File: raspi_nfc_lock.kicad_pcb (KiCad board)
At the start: 2 copper layers, 79 parts, among them J101 Raspberry_Pi_2_3, J102 Screw_Terminal_01x02, J103 Screw_Terminal_01x02, J104 Screw_Terminal_01x02, J105 Screw_Terminal_01x02, J106 Screw_Terminal_01x02, J107 Screw_Terminal_01x02, J108 Screw_Terminal_01x02, J109 Screw_Terminal_01x02, J110 Screw_Terminal_01x02, J111 Screw_Terminal_01x02, J112 Screw_Terminal_01x02, J113 BUZZER, K101 G6E, Q101 MMBT3904, Q102 Si2319CDS, Q103 MMBT3904, U101 74HC14, U102 LM2596S, U103 TXB0104D

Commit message: Finished PCB design
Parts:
- D111: value PESD3V3L4UF -> SP0502BAHT; footprint Package_TO_SOT_SMD:SOT-886 -> Package_TO_SOT_SMD:SOT-23
- moved R129 105.7 mm to (155.5, 77.2), turned to 270 degrees
- moved J113 99.5 mm to (148.0, 64.5)
- moved Q103 98.4 mm to (153.5, 72.0), turned to 180 degrees
- moved R130 94.2 mm to (143.0, 73.5)
- moved R131 92.0 mm to (143.1, 70.5)
- moved C108 91.5 mm to (142.5, 93.2), turned to 0 degrees
- moved D108 86.1 mm to (102.0, 137.0), turned to 270 degrees
- moved D109 86.1 mm to (119.0, 131.8)
- moved R126 85.6 mm to (119.0, 126.8)
- moved R101 84.0 mm to (131.6, 115.8), turned to 90 degrees
- moved C101 83.9 mm to (143.2, 117.7)
- moved C102 83.9 mm to (143.9, 119.2)
- moved C103 83.9 mm to (145.4, 120.7)
- moved C104 83.9 mm to (150.2, 118.7)
- moved C105 83.9 mm to (151.7, 117.2)
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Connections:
- net Net-(D108-Pad1) renamed /LOCK_SOLENOID
- net Net-(F101-Pad2) renamed /PWR_IN
- net Net-(J110-Pad2) renamed /NFC_CS
- net Net-(J111-Pad1) renamed /NFC_MISO
- net Net-(J111-Pad2) renamed /NFC_MOSI
- net Net-(J112-Pad1) renamed /NFC_SCK
- net Net-(J113-Pad2) renamed /BUZZ
- D111 pad 1: /APA102_CLK -> /LED_CLK
- D111 pad 2: GND -> /LED_DATA
- D111 pad 3: /APA102_DATA -> GND
- J101 pad 32: (no net) -> /BUZZER
- J108 pad 2: Net-(J108-Pad2) -> /LED_DATA
- J109 pad 1: Net-(J109-Pad1) -> /LED_CLK
- R129 pad 2: (no net) -> /BUZZER
- R132 pad 1: Net-(J108-Pad2) -> /LED_DATA
- R133 pad 1: Net-(J109-Pad1) -> /LED_CLK
- U103 pad 8: (no net) -> +3V3
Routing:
- net +5V: track 23.3 -> 144.6 mm
- net +3V3: track 16.6 -> 113.9 mm, vias 3 -> 5
- net +12V: track 33.6 -> 123.5 mm, vias 0 -> 2
- net /DOOR_SW: track 2.13 -> 40.6 mm
- net /RELAY: track 0.00 -> 38.1 mm
- net /LOCK_SOLENOID: track 0.00 -> 34.6 mm
- net /LATCH_SW: track 3.43 -> 37.3 mm
- net /HANDLE: track 3.63 -> 30.6 mm, vias 1 -> 0
- net /DOOR: track 3.65 -> 30.6 mm, vias 1 -> 0
- net /*CE0: track 0.00 -> 26.1 mm
- net /LATCH: track 3.65 -> 29.5 mm, vias 1 -> 0
- net /HANDLE_SW: track 1.55 -> 26.3 mm
- net /BUTTON_1: track 4.78 -> 27.6 mm
- net /B1: track 3.89 -> 26.5 mm, vias 1 -> 2
- net /BUTTON_2: track 4.14 -> 25.8 mm
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- added copper zone on F.Cu, net GND

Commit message: Cleanups
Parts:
- D101, D108: footprint Diodes_SMD:D_SMB -> Diodes_SMD:D_SOD-123
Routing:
- net Net-(D101-Pad2): track 18.7 -> 16.1 mm, vias 1 -> 0

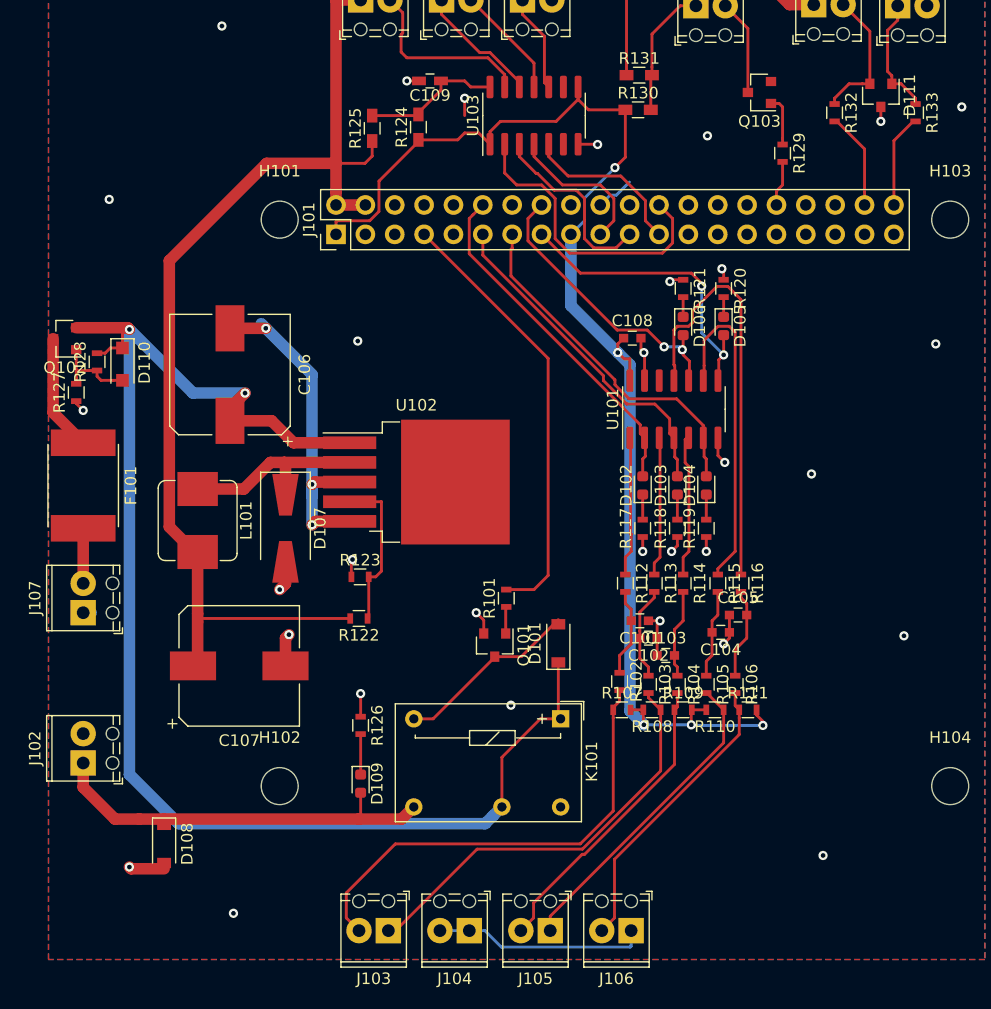
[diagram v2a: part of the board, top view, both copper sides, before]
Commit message: Moved silkprints away from pads
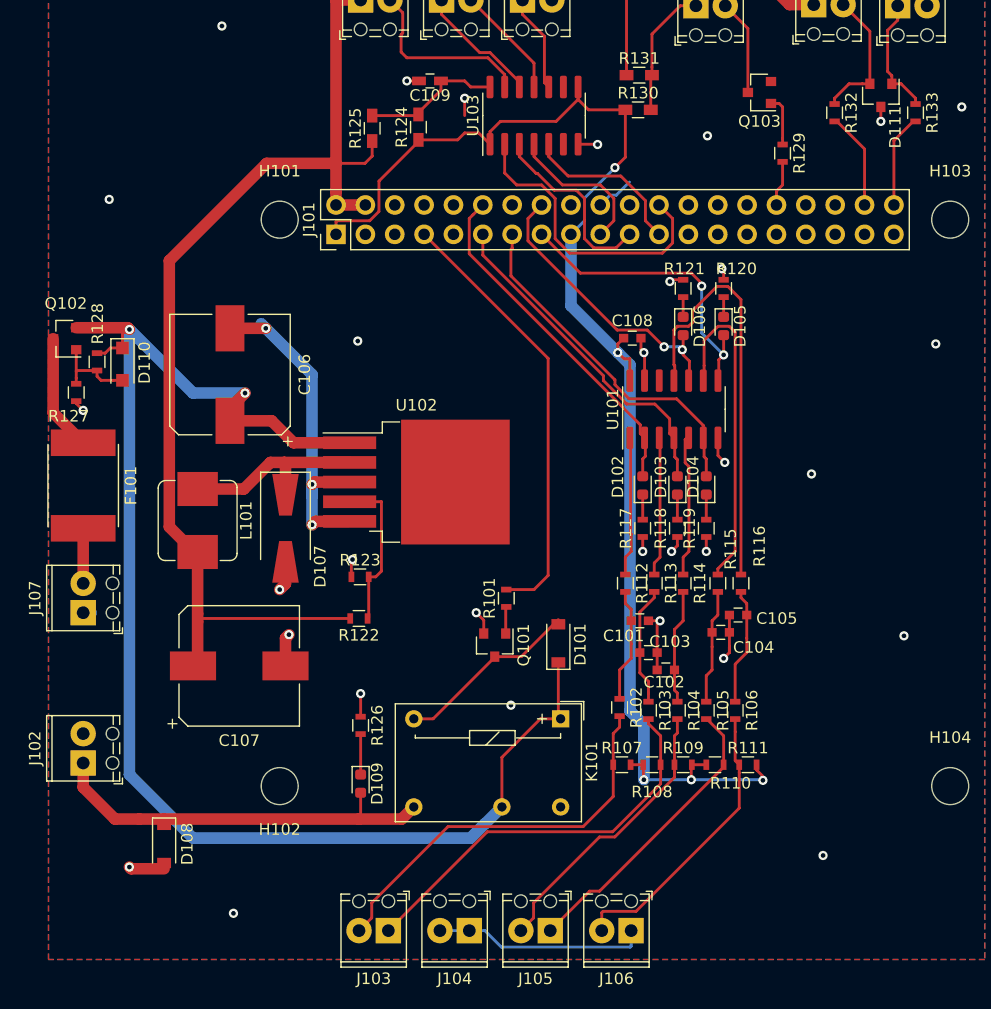
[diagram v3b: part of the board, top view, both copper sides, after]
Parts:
- moved R107 4.75 mm to (141.6, 130.2)
- moved R108 4.75 mm to (144.2, 130.2)
- moved R109 4.75 mm to (146.9, 130.2)
- moved R110 4.75 mm to (149.7, 130.2)
- moved R111 4.75 mm to (152.5, 130.2)
- moved R102 2.25 mm to (141.4, 125.2)
- moved R103 2.25 mm to (143.9, 125.5)
- moved R104 2.25 mm to (146.4, 125.5)
- moved R105 2.25 mm to (148.9, 125.5)
- moved R106 2.25 mm to (151.4, 125.5)
- moved C102 1.25 mm to (143.9, 120.5)
- moved C103 1.25 mm to (145.4, 122.0)
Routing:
- net /DOOR_SW: track 40.6 -> 35.1 mm
- net +3V3: track 113.9 -> 118.7 mm
- net GND: track 92.4 -> 95.4 mm
- net /LATCH_SW: track 37.3 -> 34.8 mm
- net Net-(C103-Pad2): track 7.66 -> 9.91 mm
- net Net-(C104-Pad2): track 7.66 -> 9.91 mm
- net Net-(C102-Pad2): track 8.08 -> 10.3 mm
- net Net-(C105-Pad2): track 7.87 -> 10.1 mm
- net Net-(C101-Pad2): track 7.62 -> 9.87 mm
- net /BUTTON_1: track 27.6 -> 25.7 mm
- net /HANDLE_SW: track 26.3 -> 24.7 mm
- net +12V: track 123.5 -> 124.5 mm
- net /BUTTON_2: track 25.8 -> 25.2 mm

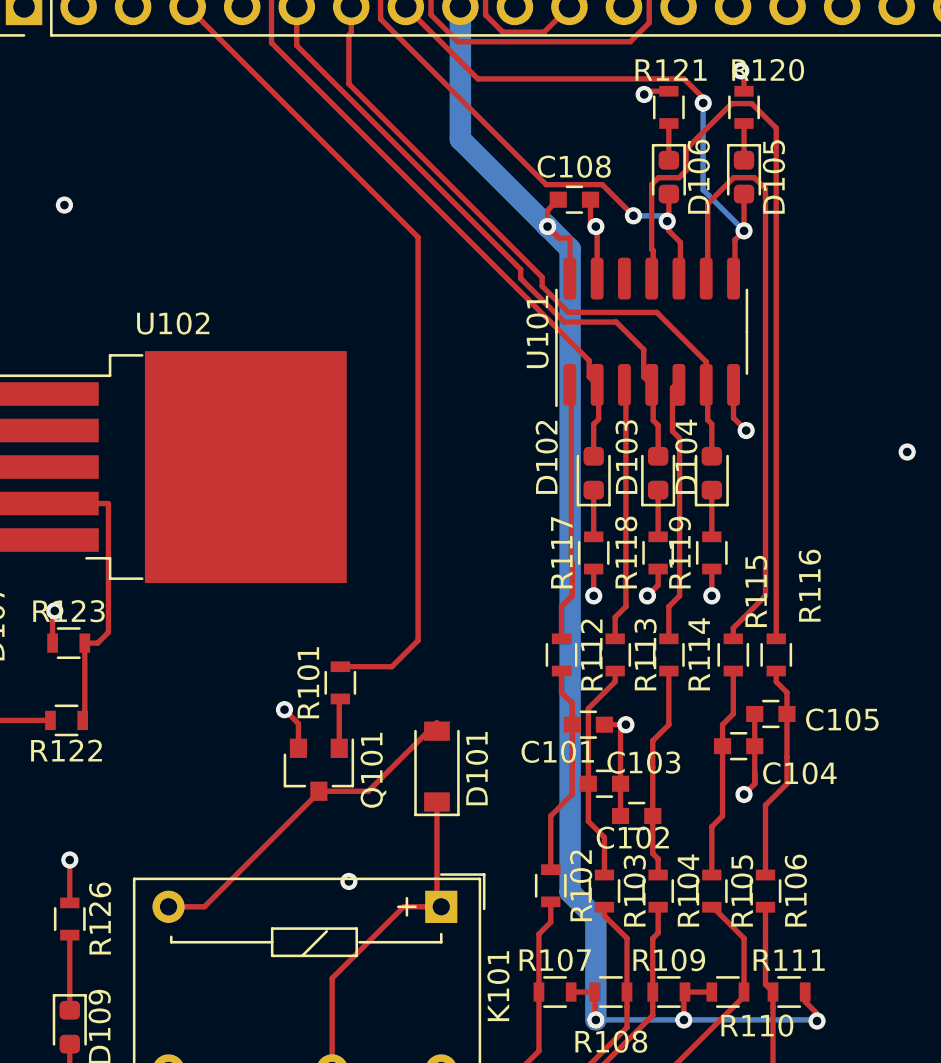
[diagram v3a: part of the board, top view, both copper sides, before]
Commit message: Removed thermals from regulator
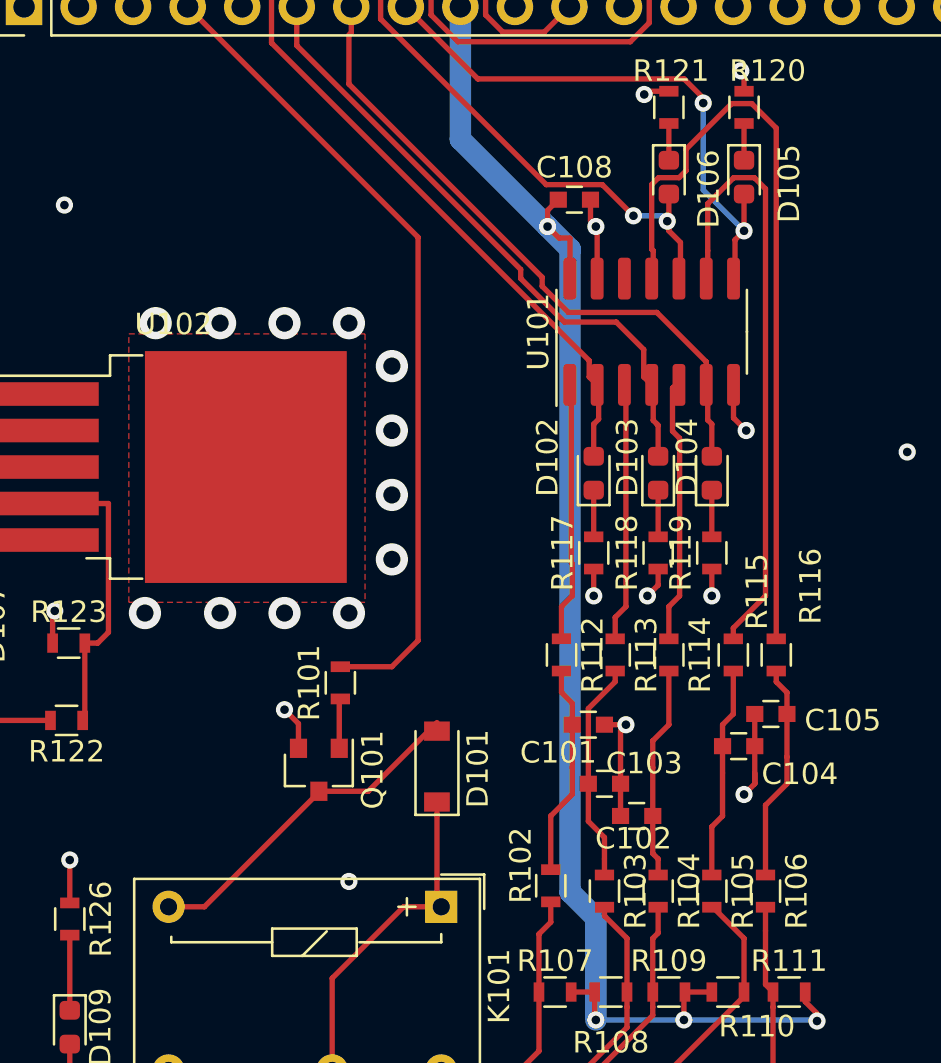
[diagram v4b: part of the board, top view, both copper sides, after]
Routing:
- net GND: vias 35 -> 47
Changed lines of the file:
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@@
     (thickness 1.6)
     (drawings 4)
-    (tracks 521)
+    (tracks 533)
     (zones 0)
     (modules 79)
@@
   (page A4)
   (layers
-    (0 F.Cu signal hide)
-    (31 B.Cu signal hide)
+    (0 F.Cu signal)
+    (31 B.Cu signal)
     (32 B.Adhes user)
     (33 F.Adhes user)
@@
     (tags "resistor 0603")
     (attr smd)
-    (fp_text reference R102 (at 0 -1.45 90) (layer F.SilkS)
+    (fp_text reference R102 (at -0.95 1.4 90) (layer F.SilkS)
       (effects (font (size 1 1) (thickness 0.15)))
     )
@@
     (tags diode)
     (attr smd)
-    (fp_text reference D106 (at 0 -1.43 90) (layer F.SilkS)
+    (fp_text reference D106 (at 0.55 -1.85 90) (layer F.SilkS)
       (effects (font (size 1 1) (thickness 0.15)))
     )
@@
     (tags diode)
     (attr smd)
-    (fp_text reference D105 (at 0 -1.43 90) (layer F.SilkS)
+    (fp_text reference D105 (at 0.3 -2.1 90) (layer F.SilkS)
       (effects (font (size 1 1) (thickness 0.15)))
     )
@@
   (segment (start 144.65 117.95) (end 144.9 117.7) (width 0.25) (layer F.Cu) (net 3))
   (segment (start 144.65 120.45) (end 144.65 117.95) (width 0.25) (layer F.Cu) (net 3))
+  (via (at 123 99) (size 1.5) (drill 0.8) (layers F.Cu B.Cu) (net 3))
+  (via (at 126 99) (size 1.5) (drill 0.8) (layers F.Cu B.Cu) (net 3))
+  (via (at 129 99) (size 1.5) (drill 0.8) (layers F.Cu B.Cu) (net 3))
+  (via (at 132 99) (size 1.5) (drill 0.8) (layers F.Cu B.Cu) (net 3))
+  (via (at 134 101) (size 1.5) (drill 0.8) (layers F.Cu B.Cu) (net 3))
+  (via (at 134 104) (size 1.5) (drill 0.8) (layers F.Cu B.Cu) (net 3))
+  (via (at 134 107) (size 1.5) (drill 0.8) (layers F.Cu B.Cu) (net 3))
+  (via (at 134 110) (size 1.5) (drill 0.8) (layers F.Cu B.Cu) (net 3))
+  (via (at 132 112.5) (size 1.5) (drill 0.8) (layers F.Cu B.Cu) (net 3))
+  (via (at 129 112.5) (size 1.5) (drill 0.8) (layers F.Cu B.Cu) (net 3))
+  (via (at 126 112.5) (size 1.5) (drill 0.8) (layers F.Cu B.Cu) (net 3))
+  (via (at 122.5 112.5) (size 1.5) (drill 0.8) (layers F.Cu B.Cu) (net 3))
   (segment (start 142.35 130.15) (end 143.45 130.15) (width 0.25) (layer F.Cu) (net 4) (status 30))
   (via (at 143.5 131.45) (size 0.8) (drill 0.4) (layers F.Cu B.Cu) (net 4))
@@
   (segment (start 118.05 104) (end 112.4 104) (width 1) (layer F.Cu) (net 31) (status 10))
   (segment (start 119 131) (end 119 127.5) (width 0.25) (layer F.Cu) (net 32) (status 30))
-  (segment (start 95 114.46) (end 95 109.7) (width 1) (layer F.Cu) (net 53) (status 30))
   (segment (start 92.4 99.7) (end 95 102.3) (width 1) (layer F.Cu) (net 33) (status 20))
   (segment (start 92.4 93.3) (end 92.4 99.7) (width 1) (layer F.Cu) (net 33) (status 10))
@@
   (segment (start 119 132.575) (end 119 134.7) (width 0.25) (layer F.Cu) (net 52) (status 10))
   (segment (start 122.55 134.85) (end 118.85 134.85) (width 1) (layer F.Cu) (net 52))
+  (segment (start 95 114.46) (end 95 109.7) (width 1) (layer F.Cu) (net 53) (status 30))
   (segment (start 163.05 66.71) (end 163.05 71.25) (width 0.25) (layer F.Cu) (net 54) (status 20))
   (segment (start 160.74 64.4) (end 163.05 66.71) (width 0.25) (layer F.Cu) (net 54) (status 10))
@@
       )
     )
+  )
+  (zone (net 3) (net_name GND) (layer F.Cu) (hatch edge 0.508)
+    (connect_pads thru_hole_only (clearance 0.5))
+    (min_thickness 0.254)
+    (fill yes (arc_segments 32) (thermal_gap 0.508) (thermal_bridge_width 0.508))
+    (polygon
+      (pts
+        (xy 121.75 99.5) (xy 132.75 99.5) (xy 132.75 112) (xy 121.75 112)
+      )
+    )

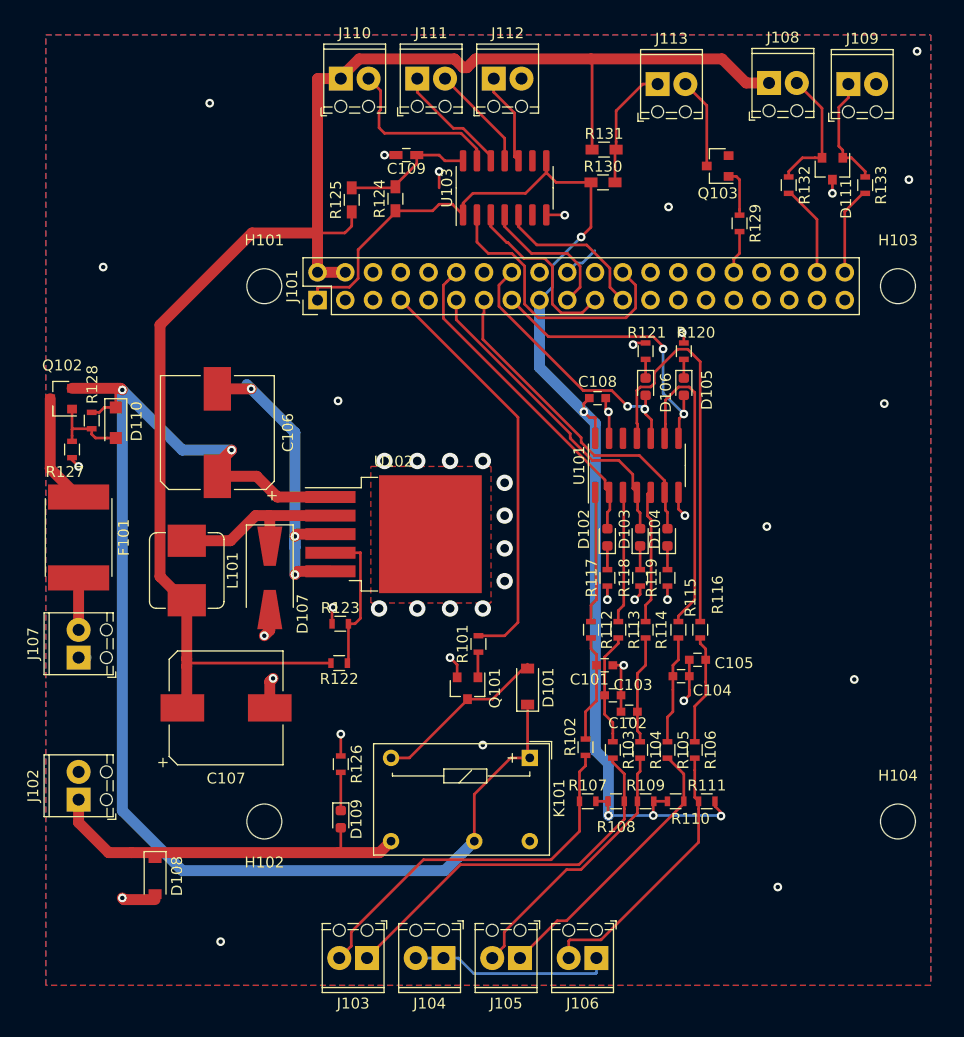
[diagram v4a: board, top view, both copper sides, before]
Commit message: Changed TX0104 to TSSOP
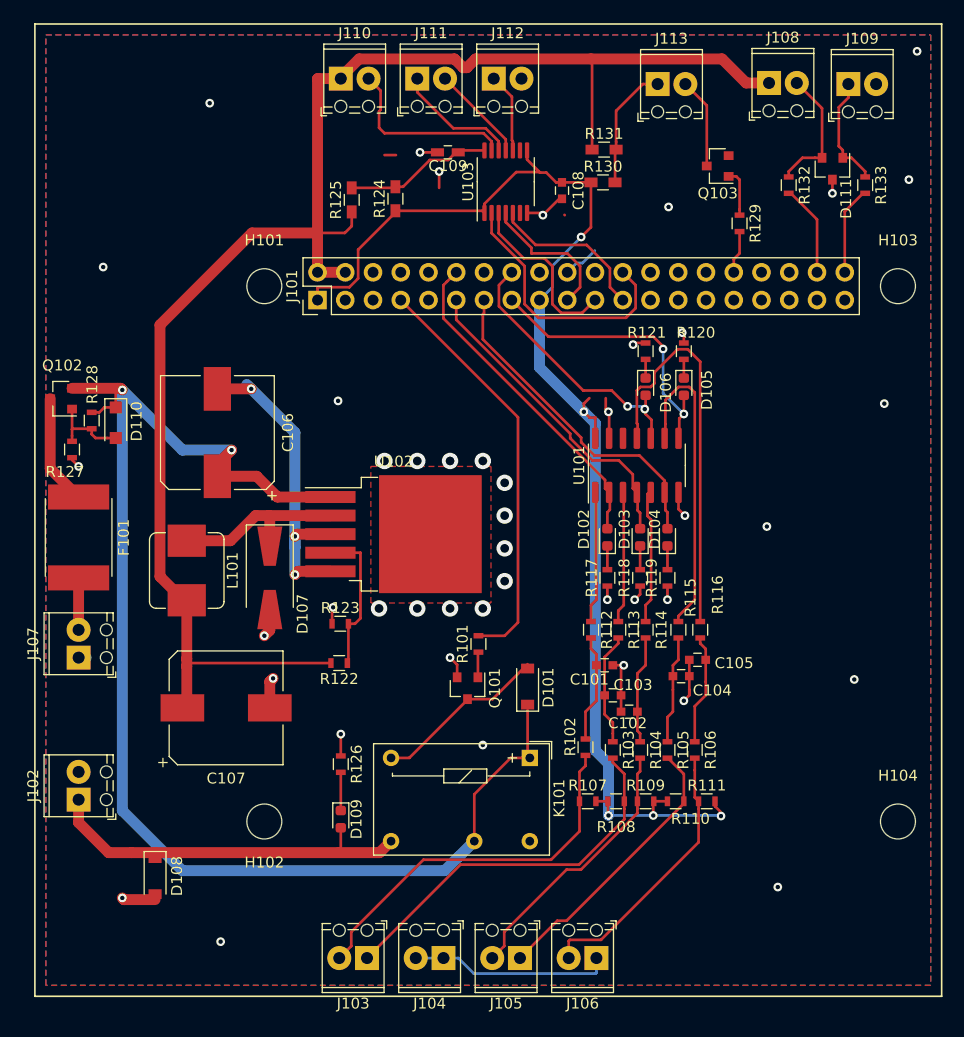
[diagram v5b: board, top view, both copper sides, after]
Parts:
- R124: value 0R -> DNI
- R125: value DNI -> 0R
- U103: value TXB0104D -> TXB0104PW; footprint Package_SO:SOIC-14_3.9x8.7mm_P1.27mm -> Package_SO:TSSOP-14_4.4x5mm_P0.65mm
- moved C108 19.3 mm to (139.2, 74.2), turned to 270 degrees
- moved C109 3.81 mm to (128.8, 70.8)
- moved U103 0.57 mm to (134.1, 73.4)
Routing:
- net GND: track 95.4 -> 99.2 mm
- net /*CE0: track 26.1 -> 24.4 mm
- net Net-(C109-Pad1): track 12.2 -> 13.6 mm
- net /NFC_SCK: track 8.47 -> 7.30 mm
- net /NFC_MOSI: track 9.79 -> 8.88 mm
- net /NFC_CS: track 15.9 -> 16.7 mm
- net +3V3: track 118.7 -> 119.3 mm
- net /NFC_MISO: track 10.8 -> 11.4 mm
